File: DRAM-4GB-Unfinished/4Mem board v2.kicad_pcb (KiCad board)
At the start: 6 copper layers, 150.4 x 75.2 mm, 29 parts, among them P1 CONN_1, P11 CONN_2X2, P2 CONN_1, P3 CONN_1, P4 CONN_1, P8 CONN_20X2, P9 CONN_20X2, U1 XC6SLX45-2FGG484C, U2 DDR3_DIMM_240PIN, U7 LM1086CS_TO252_DPAK

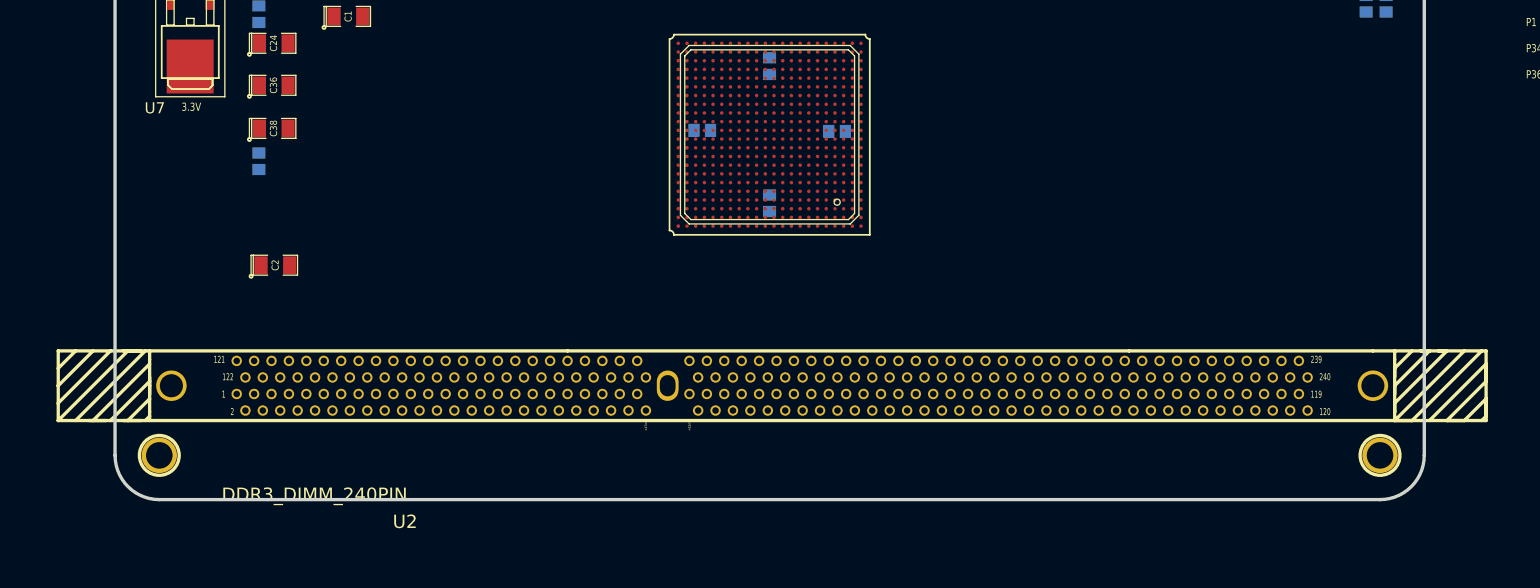
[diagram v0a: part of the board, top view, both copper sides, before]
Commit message: DRAM-4GB-Unfinished: wire DDR3 DIMM address, data and strobes to the FPGA
Source: S100 4GB DRAM BOARD/4Mem board v2/backups/03-05-2015 2323
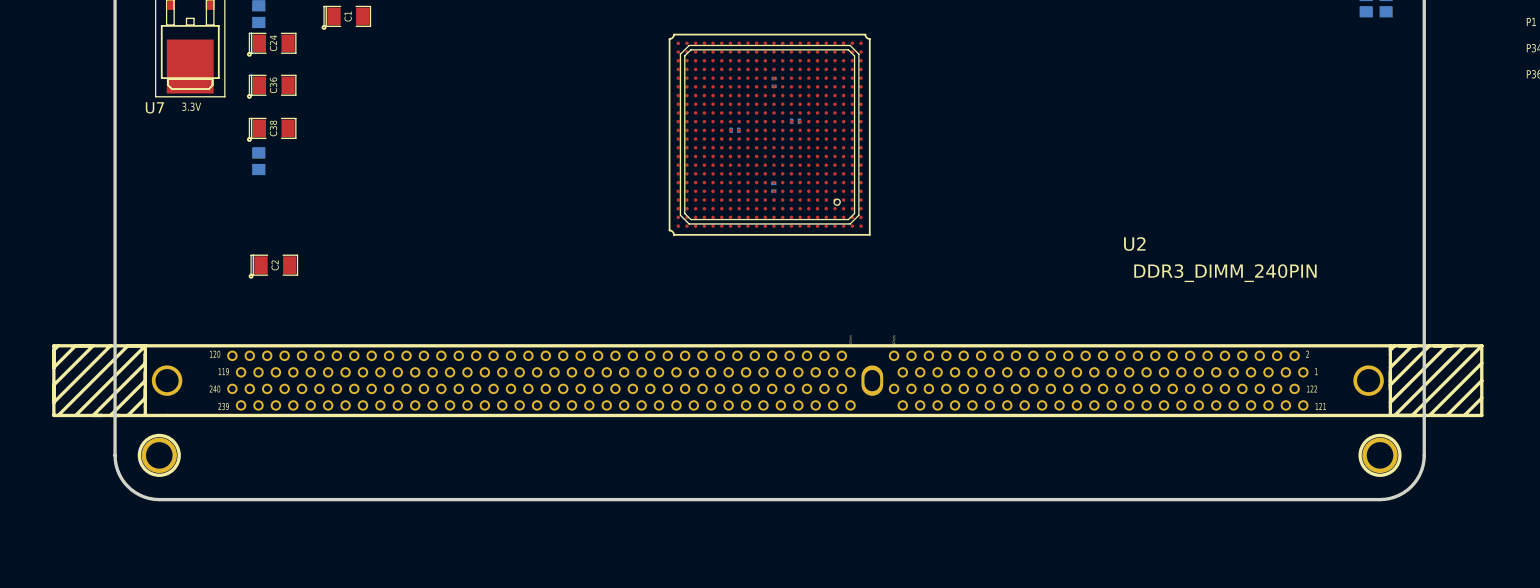
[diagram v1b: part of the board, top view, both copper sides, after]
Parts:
- C14, C27, C4, C6: footprint ^^SMD_Resistor-0805 -> SM0402_c
- moved U2 122.5 mm to (241.0, 139.0), turned to 180 degrees
- moved C6 4.91 mm to (182.7, 109.2), turned to 180 degrees
- moved C4 3.76 mm to (175.7, 110.2)
- moved C14 1.93 mm to (180.2, 104.7)
- moved C27 1.90 mm to (180.2, 116.8)
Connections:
- U1 pad A2: (no net) -> /DDR3_A3
- U1 pad A20: (no net) -> /DDR3_A2
- U1 pad A21: (no net) -> /DDR3_A1
- U1 pad B1: (no net) -> /DDR3_DQ31
- U1 pad B2: (no net) -> /DDR3_DQ27
- U1 pad B21: (no net) -> /DDR3_CK1h
- U1 pad B22: (no net) -> /DDR3_CK1l
- U1 pad C1: (no net) -> /DDR3_DQ30
- U1 pad C19: (no net) -> /DDR3_DQ36
- U1 pad C20: (no net) -> /DDR3_DQ33
- U1 pad C22: (no net) -> /DDR3_DQ32
- U1 pad C3: (no net) -> /DDR3_DQ26
- U1 pad D1: (no net) -> /DDR3_DQS3l
- U1 pad D19: (no net) -> /DDR3_DQS4h
- U1 pad D2: (no net) -> /DDR3_DQS3h
- U1 pad D20: (no net) -> /DDR3_DQS4l
- U1 pad D21: (no net) -> /DDR3_DQ37
- U1 pad D22: (no net) -> /DDR3_DM4
- U1 pad E1: (no net) -> /DDR3_DQ25
- U1 pad E20: (no net) -> /DDR3_DQ34
- U1 pad E22: (no net) -> /DDR3_DQ38
- U1 pad E3: (no net) -> /DDR3_DM3
- U1 pad F1: (no net) -> /DDR3_DQ24
- U1 pad F18: (no net) -> /DDR3_CK0h
- U1 pad F19: (no net) -> /DDR3_CK0l
- U1 pad F2: (no net) -> /DDR3_DQ29
- U1 pad F20: (no net) -> /DDR3_DQ44
- U1 pad F21: (no net) -> /DDR3_DQ39
- U1 pad F22: (no net) -> /DDR3_DQ35
- U1 pad F3: (no net) -> /DDR3_DQ28
- U1 pad F5: (no net) -> /DDR3_A6
- U1 pad G1: (no net) -> /DDR3_DQ19
- U1 pad G19: (no net) -> /DDR3_A0
- U1 pad G20: (no net) -> /DDR3_DQ45
- U1 pad G22: (no net) -> /DDR3_DQ40
- U1 pad G3: (no net) -> /DDR3_DQ23
- U1 pad G4: (no net) -> /DDR3_A7
- U1 pad G6: (no net) -> /DDR3_A5
- U1 pad H1: (no net) -> /DDR3_DQ22
- U1 pad H18: (no net) -> /DDR3_BA1
- U1 pad H19: (no net) -> /DDR3_A10
- U1 pad H2: (no net) -> /DDR3_DQ18
- U1 pad H20: (no net) -> /DDR3_DQS5l
- U1 pad H21: (no net) -> /DDR3_DQ41
- U1 pad H22: (no net) -> /DDR3_DM5
- U1 pad H3: (no net) -> /DDR3_DQS2h
- U1 pad H4: (no net) -> /DDR3_DQS2l
- U1 pad H5: (no net) -> /DDR3_A11
- U1 pad H6: (no net) -> /DDR3_A8
- U1 pad H8: (no net) -> /DDR3_A4
- U1 pad J1: (no net) -> /DDR3_DM2
- U1 pad J17: (no net) -> /DDR3_BA0
- U1 pad J19: (no net) -> /DDR3_DQS5h
- U1 pad J20: (no net) -> /DDR3_DQ42
- U1 pad J22: (no net) -> /DDR3_DQ46
- U1 pad J3: (no net) -> /DDR3_DQ21
- U1 pad J4: (no net) -> /DDR3_BA2
- U1 pad J6: (no net) -> /DDR3_A12
- U1 pad J7: (no net) -> /DDR3_A9
- U1 pad K1: (no net) -> /DDR3_DQ16
- U1 pad K17: (no net) -> /DDR3_RAS
- U1 pad K18: (no net) -> /DDR3_CAS
- U1 pad K19: (no net) -> /DDR3_S0l
- U1 pad K2: (no net) -> /DDR3_DQ17
- U1 pad K20: (no net) -> /DDR3_WE
- U1 pad K21: (no net) -> /DDR3_DQ43
- U1 pad K22: (no net) -> /DDR3_DQ47
- U1 pad K3: (no net) -> /DDR3_A15
- U1 pad K4: (no net) -> /DDR3_A14
- U1 pad K5: (no net) -> /DDR3_CKE0
- U1 pad K6: (no net) -> /DDR3_CKE1
- U1 pad L1: (no net) -> /DDR3_DQ11
- U1 pad L17: (no net) -> /DDR3_S1l
- U1 pad L19: (no net) -> /DDR3_ODT0
- U1 pad L20: (no net) -> /DDR3_DQ48
- U1 pad L22: (no net) -> /DDR3_DQ52
- U1 pad L3: (no net) -> /DDR3_DQ15
- U1 pad M1: (no net) -> /DDR3_DQ10
- U1 pad M19: (no net) -> /DDR3_DM6
- U1 pad M2: (no net) -> /DDR3_DQ14
- U1 pad M20: (no net) -> /DDR3_A13
- U1 pad M21: (no net) -> /DDR3_DQ49
- U1 pad M22: (no net) -> /DDR3_DQ53
- U1 pad M5: (no net) -> /DDR3_DQ20
- U1 pad N1: (no net) -> /DDR3_DQS1h
- U1 pad N20: (no net) -> /DDR3_DQS6h
- U1 pad N22: (no net) -> /DDR3_DQS6l
- U1 pad N3: (no net) -> /DDR3_DQS1l
- U1 pad P1: (no net) -> /DDR3_DM1
- U1 pad P19: (no net) -> /DDR3_DQ60
- U1 pad P20: (no net) -> /DDR3_OFT1
- U1 pad P21: (no net) -> /DDR3_DQ50
- U1 pad P22: (no net) -> /DDR3_DQ54
- U1 pad R1: (no net) -> /DDR3_DQ13
- U1 pad R20: (no net) -> /DDR3_DQ55
- U1 pad R22: (no net) -> /DDR3_DQ51
- U1 pad R3: (no net) -> /DDR3_DQ9
- U1 pad T1: (no net) -> /DDR3_DQ3
- U1 pad T19: (no net) -> /DDR3_DQS7h
- U1 pad T2: (no net) -> /DDR3_DQ7
- U1 pad T20: (no net) -> /DDR3_DQS7l
- U1 pad T21: (no net) -> /DDR3_DQ61
- U1 pad T22: (no net) -> /DDR3_DQ56
- U1 pad T3: (no net) -> /DDR3_DQ12
- U1 pad T4: (no net) -> /DDR3_DQ8
- U1 pad U1: (no net) -> /DDR3_DQ6
- U1 pad U20: (no net) -> /DDR3_DQ57
- U1 pad U22: (no net) -> /DDR3_DM7
- U1 pad U3: (no net) -> /DDR3_DQ2
- U1 pad U4: (no net) -> /DDR3_DQS0h
- U1 pad V1: (no net) -> /DDR3_DM0
- U1 pad V2: (no net) -> /DDR3_DQ5
- U1 pad V21: (no net) -> /DDR3_DQ58
- U1 pad V22: (no net) -> /DDR3_DQ62
- U1 pad V3: (no net) -> /DDR3_DQS0l
- U1 pad W1: (no net) -> /DDR3_DQ1
- U1 pad W20: (no net) -> /DDR3_DQ63
- U1 pad W22: (no net) -> /DDR3_DQ59
- U1 pad W3: (no net) -> /DDR3_DQ0
- U1 pad Y2: (no net) -> /DDR3_DQ4
- U2 pad 10: (no net) -> /DDR3_DQ3
- U2 pad 100: (no net) -> /DDR3_DQ49
- U2 pad 102: (no net) -> /DDR3_DQS6l
- U2 pad 103: (no net) -> /DDR3_DQS6h
- U2 pad 105: (no net) -> /DDR3_DQ50
- U2 pad 106: (no net) -> /DDR3_DQ51
- U2 pad 108: (no net) -> /DDR3_DQ56
- U2 pad 109: (no net) -> /DDR3_DQ57
- U2 pad 111: (no net) -> /DDR3_DQS7l
- U2 pad 112: (no net) -> /DDR3_DQS7h
- U2 pad 114: (no net) -> /DDR3_DQ58
- U2 pad 115: (no net) -> /DDR3_DQ59
- U2 pad 12: (no net) -> /DDR3_DQ8
- U2 pad 122: (no net) -> /DDR3_DQ4
- U2 pad 123: (no net) -> /DDR3_DQ5
- U2 pad 125: (no net) -> /DDR3_DM0
- U2 pad 128: (no net) -> /DDR3_DQ6
- U2 pad 129: (no net) -> /DDR3_DQ7
- U2 pad 13: (no net) -> /DDR3_DQ9
- U2 pad 131: (no net) -> /DDR3_DQ12
- U2 pad 132: (no net) -> /DDR3_DQ13
- U2 pad 134: (no net) -> /DDR3_DM1
- U2 pad 137: (no net) -> /DDR3_DQ14
- U2 pad 138: (no net) -> /DDR3_DQ15
- U2 pad 140: (no net) -> /DDR3_DQ20
- U2 pad 141: (no net) -> /DDR3_DQ21
- U2 pad 143: (no net) -> /DDR3_DM2
- U2 pad 146: (no net) -> /DDR3_DQ22
- U2 pad 147: (no net) -> /DDR3_DQ23
- U2 pad 149: (no net) -> /DDR3_DQ28
- U2 pad 15: (no net) -> /DDR3_DQS1l
- U2 pad 150: (no net) -> /DDR3_DQ29
- U2 pad 152: (no net) -> /DDR3_DM3
- U2 pad 155: (no net) -> /DDR3_DQ30
- U2 pad 156: (no net) -> /DDR3_DQ31
- U2 pad 16: (no net) -> /DDR3_DQS1h
- U2 pad 169: (no net) -> /DDR3_CKE1
- U2 pad 171: (no net) -> /DDR3_A15
- U2 pad 172: (no net) -> /DDR3_A14
- U2 pad 174: (no net) -> /DDR3_A12
- U2 pad 175: (no net) -> /DDR3_A9
- U2 pad 177: (no net) -> /DDR3_A8
- U2 pad 178: (no net) -> /DDR3_A6
- U2 pad 18: (no net) -> /DDR3_DQ10
- U2 pad 180: (no net) -> /DDR3_A3
- U2 pad 181: (no net) -> /DDR3_A1
- U2 pad 184: (no net) -> /DDR3_CK0h
- U2 pad 185: (no net) -> /DDR3_CK0l
- U2 pad 188: (no net) -> /DDR3_A0
- U2 pad 19: (no net) -> /DDR3_DQ11
- U2 pad 190: (no net) -> /DDR3_BA1
- U2 pad 192: (no net) -> /DDR3_RAS
- U2 pad 193: (no net) -> /DDR3_S0l
- U2 pad 195: (no net) -> /DDR3_ODT0
- U2 pad 196: (no net) -> /DDR3_A13
- U2 pad 200: (no net) -> /DDR3_DQ36
- U2 pad 201: (no net) -> /DDR3_DQ37
- U2 pad 203: (no net) -> /DDR3_DM4
- U2 pad 206: (no net) -> /DDR3_DQ38
- U2 pad 207: (no net) -> /DDR3_DQ39
- U2 pad 209: (no net) -> /DDR3_DQ44
- U2 pad 21: (no net) -> /DDR3_DQ16
- U2 pad 210: (no net) -> /DDR3_DQ45
- U2 pad 212: (no net) -> /DDR3_DM5
- U2 pad 215: (no net) -> /DDR3_DQ46
- U2 pad 216: (no net) -> /DDR3_DQ47
- U2 pad 218: (no net) -> /DDR3_DQ52
- U2 pad 219: (no net) -> /DDR3_DQ53
- U2 pad 22: (no net) -> /DDR3_DQ17
- U2 pad 221: (no net) -> /DDR3_DM6
- U2 pad 224: (no net) -> /DDR3_DQ54
- U2 pad 225: (no net) -> /DDR3_DQ55
- U2 pad 227: (no net) -> /DDR3_DQ60
- U2 pad 228: (no net) -> /DDR3_DQ61
- U2 pad 230: (no net) -> /DDR3_DM7
- U2 pad 233: (no net) -> /DDR3_DQ62
- U2 pad 234: (no net) -> /DDR3_DQ63
- U2 pad 24: (no net) -> /DDR3_DQS2l
- U2 pad 241: (no net) -> GND
- U2 pad 242: (no net) -> GND
- U2 pad 243: (no net) -> GND
- U2 pad 25: (no net) -> /DDR3_DQS2h
- U2 pad 27: (no net) -> /DDR3_DQ18
- U2 pad 28: (no net) -> /DDR3_DQ19
- U2 pad 3: (no net) -> /DDR3_DQ0
- U2 pad 30: (no net) -> /DDR3_DQ24
- U2 pad 31: (no net) -> /DDR3_DQ25
- U2 pad 33: (no net) -> /DDR3_DQS3l
- U2 pad 34: (no net) -> /DDR3_DQS3h
- U2 pad 36: (no net) -> /DDR3_DQ26
- U2 pad 37: (no net) -> /DDR3_DQ27
- U2 pad 4: (no net) -> /DDR3_DQ1
- U2 pad 50: (no net) -> /DDR3_CKE0
- U2 pad 52: (no net) -> /DDR3_BA2
- U2 pad 55: (no net) -> /DDR3_A11
- U2 pad 56: (no net) -> /DDR3_A7
- U2 pad 58: (no net) -> /DDR3_A5
- U2 pad 59: (no net) -> /DDR3_A4
- U2 pad 6: (no net) -> /DDR3_DQS0l
- U2 pad 61: (no net) -> /DDR3_A2
- U2 pad 63: (no net) -> /DDR3_CK1h
- U2 pad 64: (no net) -> /DDR3_CK1l
- U2 pad 7: (no net) -> /DDR3_DQS0h
- U2 pad 70: (no net) -> /DDR3_A10
- U2 pad 71: (no net) -> /DDR3_BA0
- U2 pad 73: (no net) -> /DDR3_WE
- U2 pad 74: (no net) -> /DDR3_CAS
- U2 pad 76: (no net) -> /DDR3_S1l
- U2 pad 77: (no net) -> /DDR3_OFT1
- U2 pad 81: (no net) -> /DDR3_DQ32
- U2 pad 82: (no net) -> /DDR3_DQ33
- U2 pad 84: (no net) -> /DDR3_DQS4l
- U2 pad 85: (no net) -> /DDR3_DQS4h
- U2 pad 87: (no net) -> /DDR3_DQ34
- U2 pad 88: (no net) -> /DDR3_DQ35
- U2 pad 9: (no net) -> /DDR3_DQ2
- U2 pad 90: (no net) -> /DDR3_DQ40
- U2 pad 91: (no net) -> /DDR3_DQ41
- U2 pad 93: (no net) -> /DDR3_DQS5l
- U2 pad 94: (no net) -> /DDR3_DQS5h
- U2 pad 96: (no net) -> /DDR3_DQ42
- U2 pad 97: (no net) -> /DDR3_DQ43
- U2 pad 99: (no net) -> /DDR3_DQ48
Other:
- net class gnd: clearance 0.1905 -> 0.1016; trace_width 0.35 -> 0.45
